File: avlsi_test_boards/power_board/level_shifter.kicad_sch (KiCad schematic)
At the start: 10 parts, among them U9 SN74LVC16T245DLR

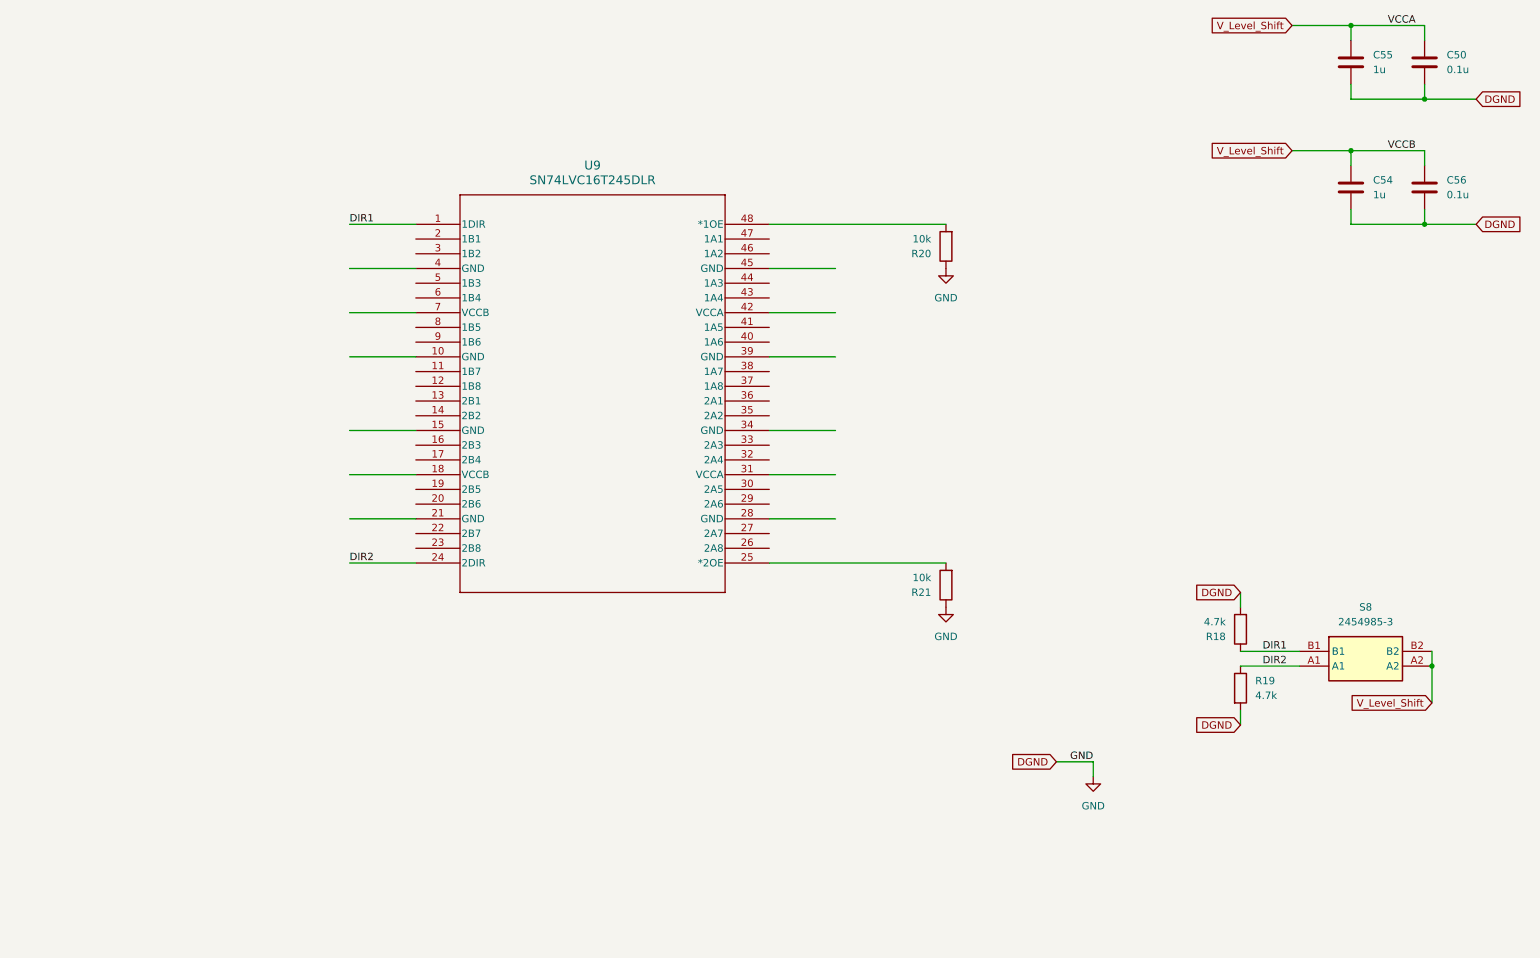
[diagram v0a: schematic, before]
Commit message: Add updated schematic
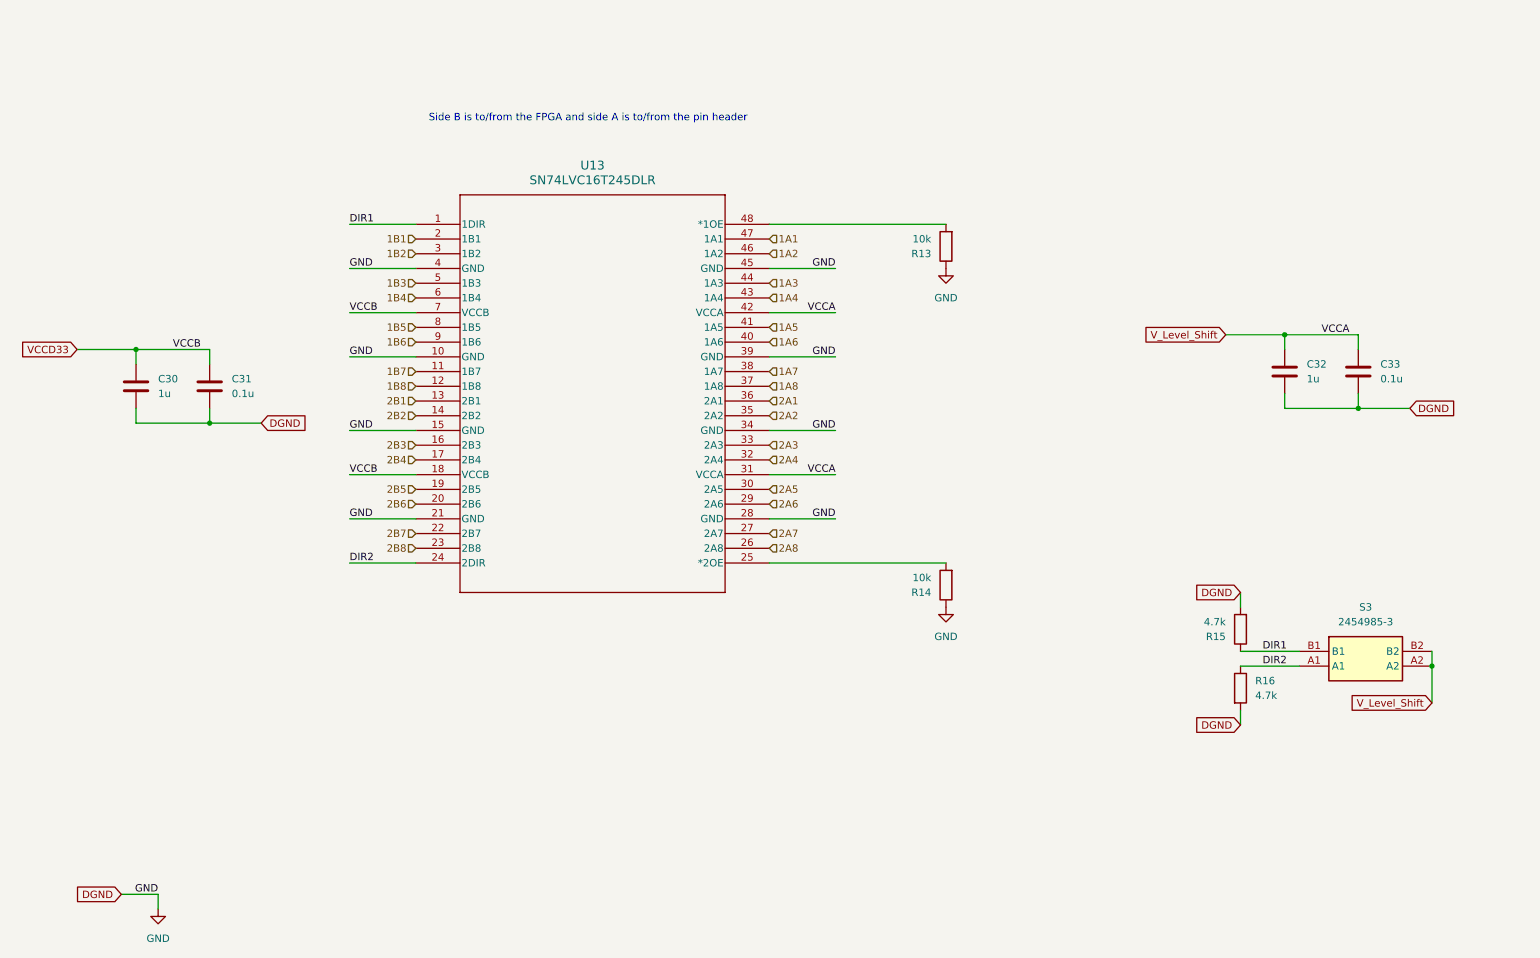
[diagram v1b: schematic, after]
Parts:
- renumbered C54 to C30, C56 to C31, C55 to C32, C50 to C33, R20 to R13, R21 to R14, R18 to R15, R19 to R16, S8 to S3, U9 to U13
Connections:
- net GND: now also U13.10 (GND), U13.15 (GND), U13.21 (GND), U13.28 (GND), U13.34 (GND), U13.39 (GND), U13.4 (GND), U13.45 (GND)
- net V_Level_Shift: now also U13.31 (VCCA), U13.42 (VCCA); no longer C30.1, C31.1
- net 1B7: now reaches U13.11 (1B7)
- net 1B8: now reaches U13.12 (1B8)
- net 2B1: now reaches U13.13 (2B1)
- net 2B2: now reaches U13.14 (2B2)
- net 2B3: now reaches U13.16 (2B3)
- net 2B4: now reaches U13.17 (2B4)
- net VCCD33: now reaches U13.18 (VCCB)
- net VCCD33: now also C30.1, C31.1, U13.7 (VCCB)
- net 2B5: now reaches U13.19 (2B5)
- net 1B1: now reaches U13.2 (1B1)
- net 2B6: now reaches U13.20 (2B6)
- net 2B7: now reaches U13.22 (2B7)
- net 2B8: now reaches U13.23 (2B8)
- net 2A8: now reaches U13.26 (2A8)
- net 2A7: now reaches U13.27 (2A7)
- net 2A6: now reaches U13.29 (2A6)
- net 1B2: now reaches U13.3 (1B2)
- net 2A5: now reaches U13.30 (2A5)
- net 2A4: now reaches U13.32 (2A4)
- net 2A3: now reaches U13.33 (2A3)
- net 2A2: now reaches U13.35 (2A2)
- net 2A1: now reaches U13.36 (2A1)
- net 1A8: now reaches U13.37 (1A8)
- net 1A7: now reaches U13.38 (1A7)
- net 1A6: now reaches U13.40 (1A6)
- net 1A5: now reaches U13.41 (1A5)
- net 1A4: now reaches U13.43 (1A4)
- net 1A3: now reaches U13.44 (1A3)
- net 1A2: now reaches U13.46 (1A2)
- net 1A1: now reaches U13.47 (1A1)
- net 1B3: now reaches U13.5 (1B3)
- net 1B4: now reaches U13.6 (1B4)
- net 1B5: now reaches U13.8 (1B5)
- net 1B6: now reaches U13.9 (1B6)
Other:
- note added: "Side B is to/from the FPGA and side A is to/from the pin header"
- moved on the sheet: C30, C31, C32, C33

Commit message: Add initial layout stuff
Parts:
- R15, R16: footprint Resistor_SMD:R_0201_0603Metric -> Resistor_SMD:R_0805_2012Metric
- S3: footprint 24549853 -> 2_DS:24549853
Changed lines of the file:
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@@
 			)
 		)
-		(property "Footprint" "Resistor_SMD:R_0201_0603Metric"
+		(property "Footprint" "Resistor_SMD:R_0805_2012Metric"
 			(at 230.378 133.35 90)
 			(effects
@@
 			)
 		)
-		(property "Footprint" "24549853"
+		(property "Footprint" "2_DS:24549853"
 			(at 257.81 232.08 0)
 			(effects
@@
 			)
 		)
-		(property "Footprint" "Resistor_SMD:R_0201_0603Metric"
+		(property "Footprint" "Resistor_SMD:R_0805_2012Metric"
 			(at 226.822 143.51 90)
 			(effects

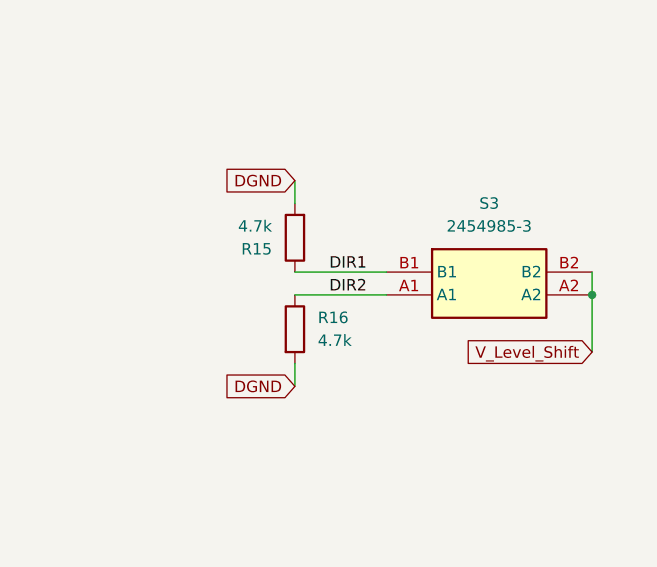
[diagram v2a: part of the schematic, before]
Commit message: Add analog power pins
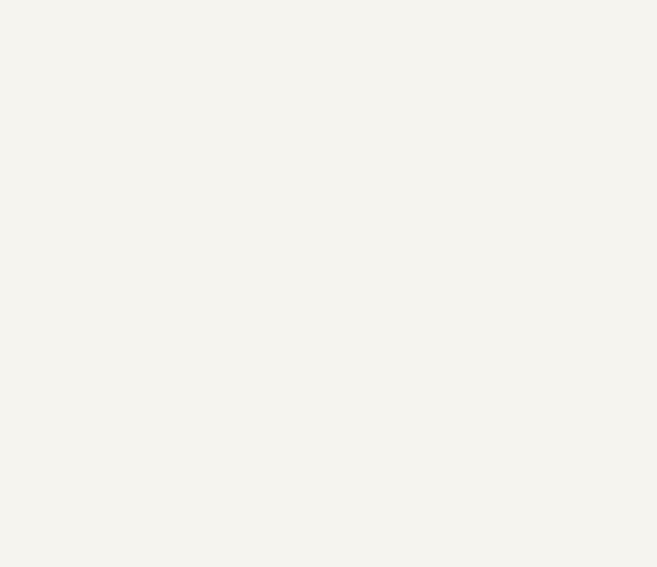
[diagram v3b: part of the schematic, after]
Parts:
- removed R15, R16: 4.7k, Resistor_SMD:R_0805_2012Metric, symbol Device:R
- removed S3: 2454985-3, 2_DS:24549853, symbol 2_DIP:2454985-3

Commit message: progress
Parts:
- added R5, R6: 4.7k, Resistor_SMD:R_0805_2012Metric, symbol Device:R
- added S1: 2454985-3, 2_DS:24549853, symbol 2_DIP:2454985-3
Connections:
- net DIR1: now also R5.1, S1.B1
- net DIR2: now also R6.1, S1.A1
- net GND: now also R5.2, R6.2
- net V_Level_Shift: now also S1.A2, S1.B2
